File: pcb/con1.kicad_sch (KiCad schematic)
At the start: 8 parts, among them J5 DIN41612_02x32_AC, U1 M24C02-WMN

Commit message: Schematic design
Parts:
- added C16: 100n, Capacitor_SMD:C_0603_1608Metric_Pad1.08x0.95mm_HandSolder, symbol Device:C
- added C17: 10u, Capacitor_SMD:C_1206_3216Metric_Pad1.33x1.80mm_HandSolder, symbol Device:C
- added U3: USBLC6-2SC6, Package_TO_SOT_SMD:SOT-23-6_Handsoldering, symbol Power_Protection:USBLC6-2SC6
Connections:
- net D+: now also U3.1 (I/O1); no longer J5.c22 (Pin_c22)
- net D-: now also U3.3 (I/O2); no longer J5.a22 (Pin_a22)
- net GND: now also C16.1, C17.2, U3.2 (GND)
- net VUSB: now also C16.2, C17.1, U3.5 (VBUS)
- new net: J5.a22 (Pin_a22), U3.4 (I/O2)
- new net: J5.c22 (Pin_c22), U3.6 (I/O1)

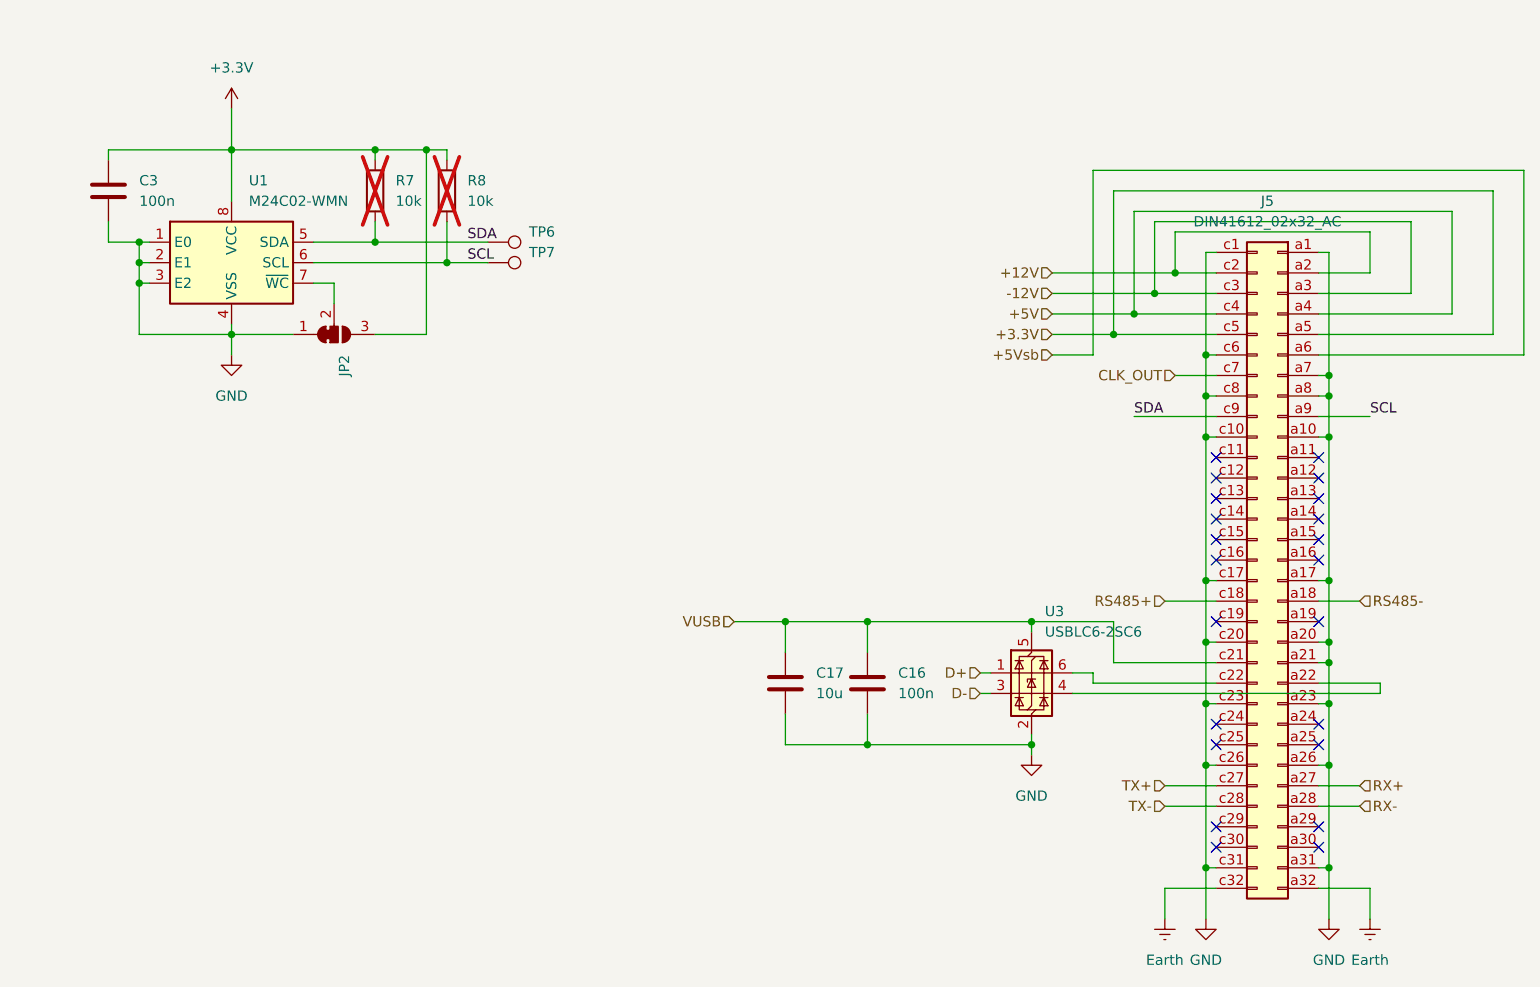
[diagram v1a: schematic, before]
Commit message: Sch complete, starting pcb
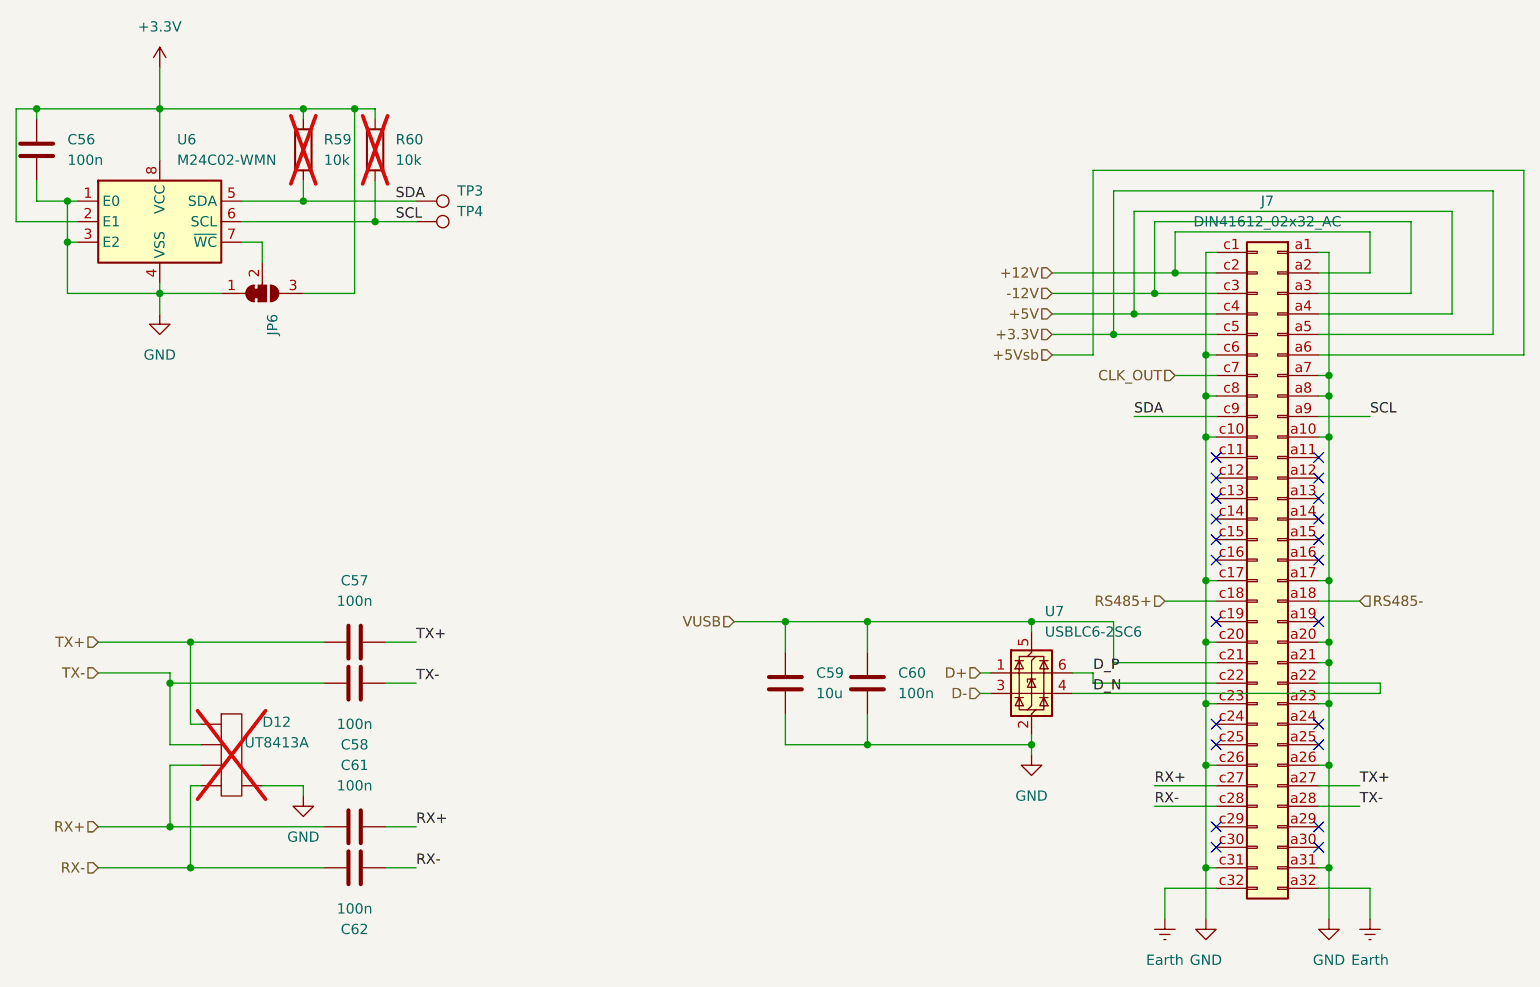
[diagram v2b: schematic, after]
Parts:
- added C57, C58, C61, C62: 100n, Capacitor_SMD:C_0805_2012Metric, symbol Device:C
- added D12: UT8413A, Package_DFN_QFN:Diodes_UDFN-10_1.0x2.5mm_P0.5mm, symbol Conn:UT8413A
- renumbered C3 to C56, C17 to C59, C16 to C60, J5 to J7, JP2 to JP6, R7 to R59, R8 to R60, TP6 to TP3, TP7 to TP4, U1 to U6, U3 to U7
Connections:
- net +3.3V: now also U6.2 (E1)
- net GND: now also D12.3, D12.8; no longer U6.2 (E1)
- net RX+: now also J7.c27 (Pin_c27), C61.1, C61.2, D12.2, D12.9; no longer J7.a27 (Pin_a27)
- net RX-: now also J7.c28 (Pin_c28), C62.1, C62.2, D12.1, D12.10; no longer J7.a28 (Pin_a28)
- net TX+: now also J7.a27 (Pin_a27), C57.1, C57.2, D12.5, D12.6; no longer J7.c27 (Pin_c27)
- net TX-: now also J7.a28 (Pin_a28), C58.1, C58.2, D12.4, D12.7; no longer J7.c28 (Pin_c28)
- net D_N: now reaches J7.a22 (Pin_a22), U7.4 (I/O2)
- net D_P: now reaches J7.c22 (Pin_c22), U7.6 (I/O1)
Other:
- moved on the sheet: C56, JP6, R59, R60, TP3, TP4, U6

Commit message: Routing
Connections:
- net +3.3V: no longer J7.a5 (Pin_a5), J7.c5 (Pin_c5)
- net RX+: no longer C61.1, J7.c27 (Pin_c27)
- net RX-: no longer C62.1, J7.c28 (Pin_c28)
- net TX+: no longer C57.1, J7.a27 (Pin_a27)
- net TX-: no longer C58.1, J7.a28 (Pin_a28)
- net +12V renamed +12V_PWR
- net +5V renamed +5V_PWR
- net -12V renamed -12V_PWR
- new net +3.3V_PWR: J7.a5 (Pin_a5), J7.c5 (Pin_c5)
- new net CON_RX+: C61.1, J7.c27 (Pin_c27)
- new net CON_RX-: C62.1, J7.c28 (Pin_c28)
- new net CON_TX+: C57.1, J7.a27 (Pin_a27)
- new net CON_TX-: C58.1, J7.a28 (Pin_a28)
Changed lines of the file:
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@@
 	(wire
 		(pts
-			(xy 226.06 111.76) (xy 233.68 111.76)
+			(xy 222.25 111.76) (xy 233.68 111.76)
 		)
 		(stroke
@@
 	(wire
 		(pts
-			(xy 226.06 109.22) (xy 233.68 109.22)
+			(xy 222.25 109.22) (xy 233.68 109.22)
 		)
 		(stroke
@@
 		)
 	)
-	(label "RX-"
-		(at 226.06 111.76 0)
+	(label "CON_RX-"
+		(at 222.25 111.76 0)
 		(effects
 			(font
@@
 		)
 	)
-	(label "TX-"
+	(label "CON_TX-"
 		(at 251.46 111.76 0)
 		(effects
@@
 		)
 	)
-	(label "TX+"
+	(label "CON_TX+"
 		(at 134.62 91.44 0)
 		(effects
@@
 		)
 	)
-	(label "RX+"
+	(label "CON_RX+"
 		(at 134.62 114.3 0)
 		(effects
@@
 		)
 	)
-	(label "RX+"
-		(at 226.06 109.22 0)
+	(label "CON_RX+"
+		(at 222.25 109.22 0)
 		(effects
 			(font
@@
 		)
 	)
-	(label "TX+"
+	(label "CON_TX+"
 		(at 251.46 109.22 0)
 		(effects
@@
 		)
 	)
-	(label "TX-"
+	(label "CON_TX-"
 		(at 134.62 96.52 0)
 		(effects
@@
 		)
 	)
-	(label "RX-"
+	(label "CON_RX-"
 		(at 134.62 119.38 0)
 		(effects
@@
 		)
 	)
-	(hierarchical_label "-12V"
+	(hierarchical_label "-12V_PWR"
 		(shape input)
 		(at 213.36 48.26 180)
@@
 		)
 	)
-	(hierarchical_label "+5V"
+	(hierarchical_label "+5V_PWR"
 		(shape input)
 		(at 213.36 50.8 180)
@@
 		)
 	)
-	(hierarchical_label "+12V"
+	(hierarchical_label "+12V_PWR"
 		(shape input)
 		(at 213.36 45.72 180)
@@
 		)
 	)
-	(hierarchical_label "+3.3V"
+	(hierarchical_label "+3.3V_PWR"
 		(shape input)
 		(at 213.36 53.34 180)
